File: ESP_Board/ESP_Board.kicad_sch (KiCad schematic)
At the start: 37 parts, among them J1 USB_C_Receptacle_USB2.0_14P, J2 Conn_01x18_Pin, J3 Conn_01x18_Pin, SW1 SW_Push, U1 ESP32-S3, U2 AMS1117, Y1 C1E-40.000-8-1010-R

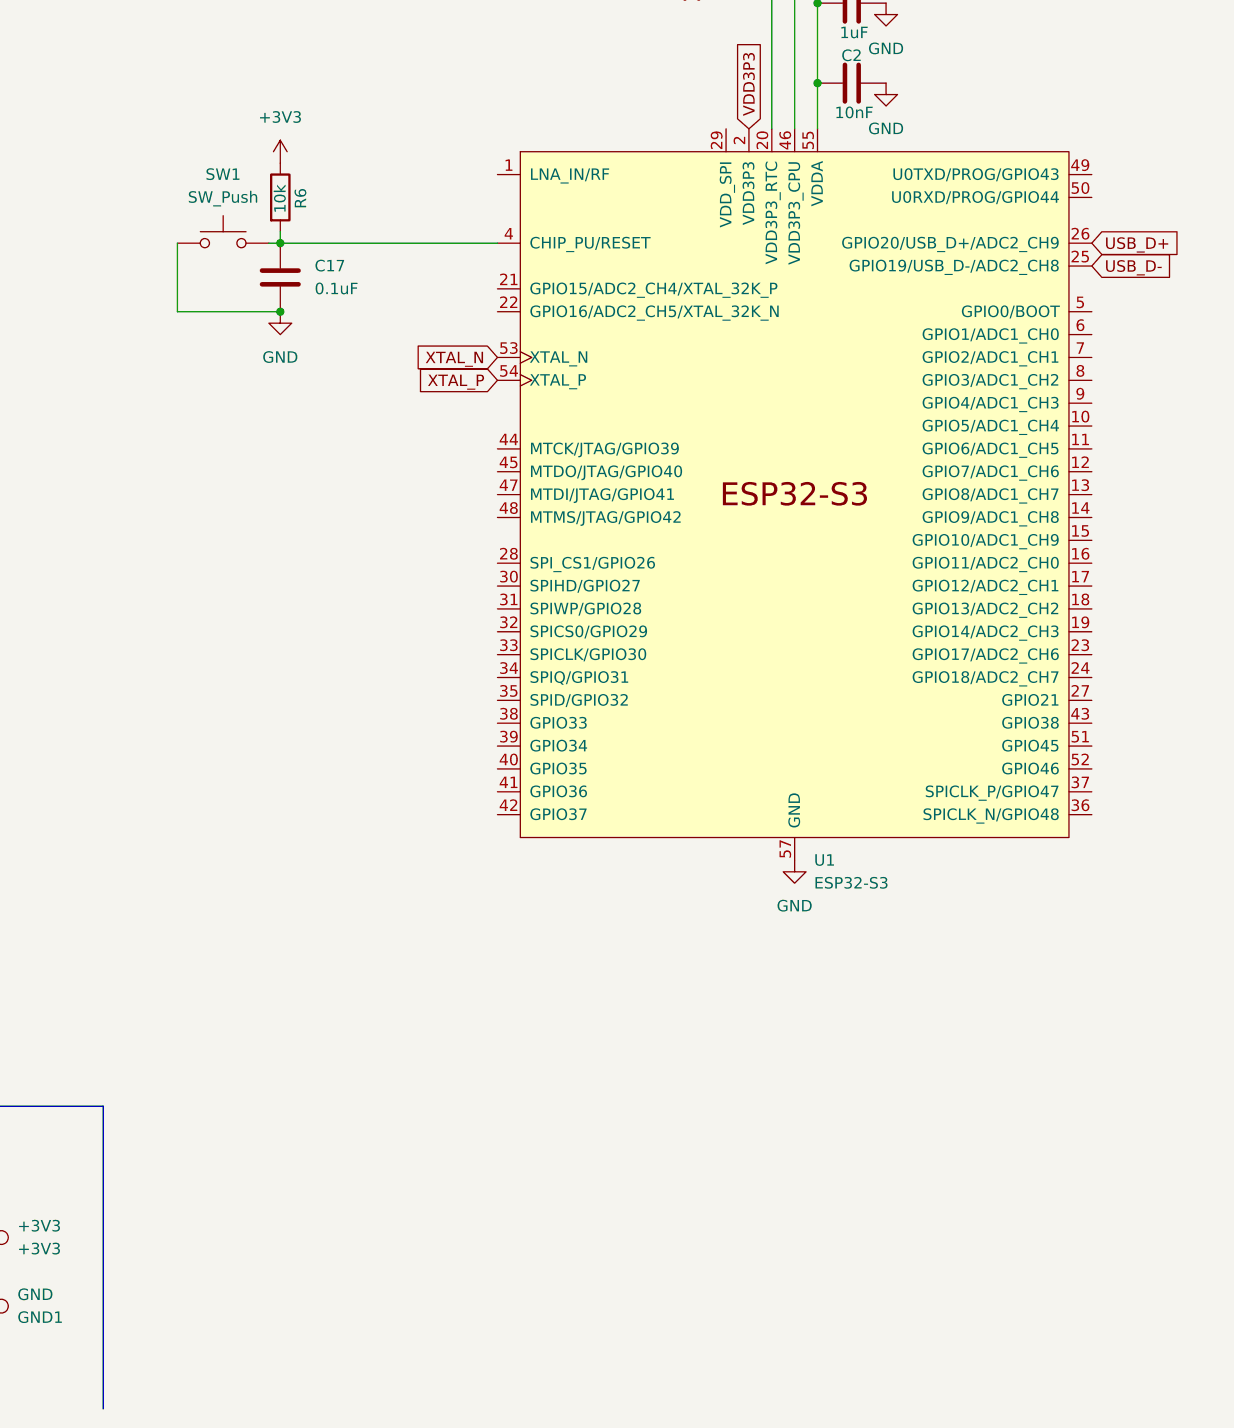
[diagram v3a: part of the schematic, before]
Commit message: Added BOOT button
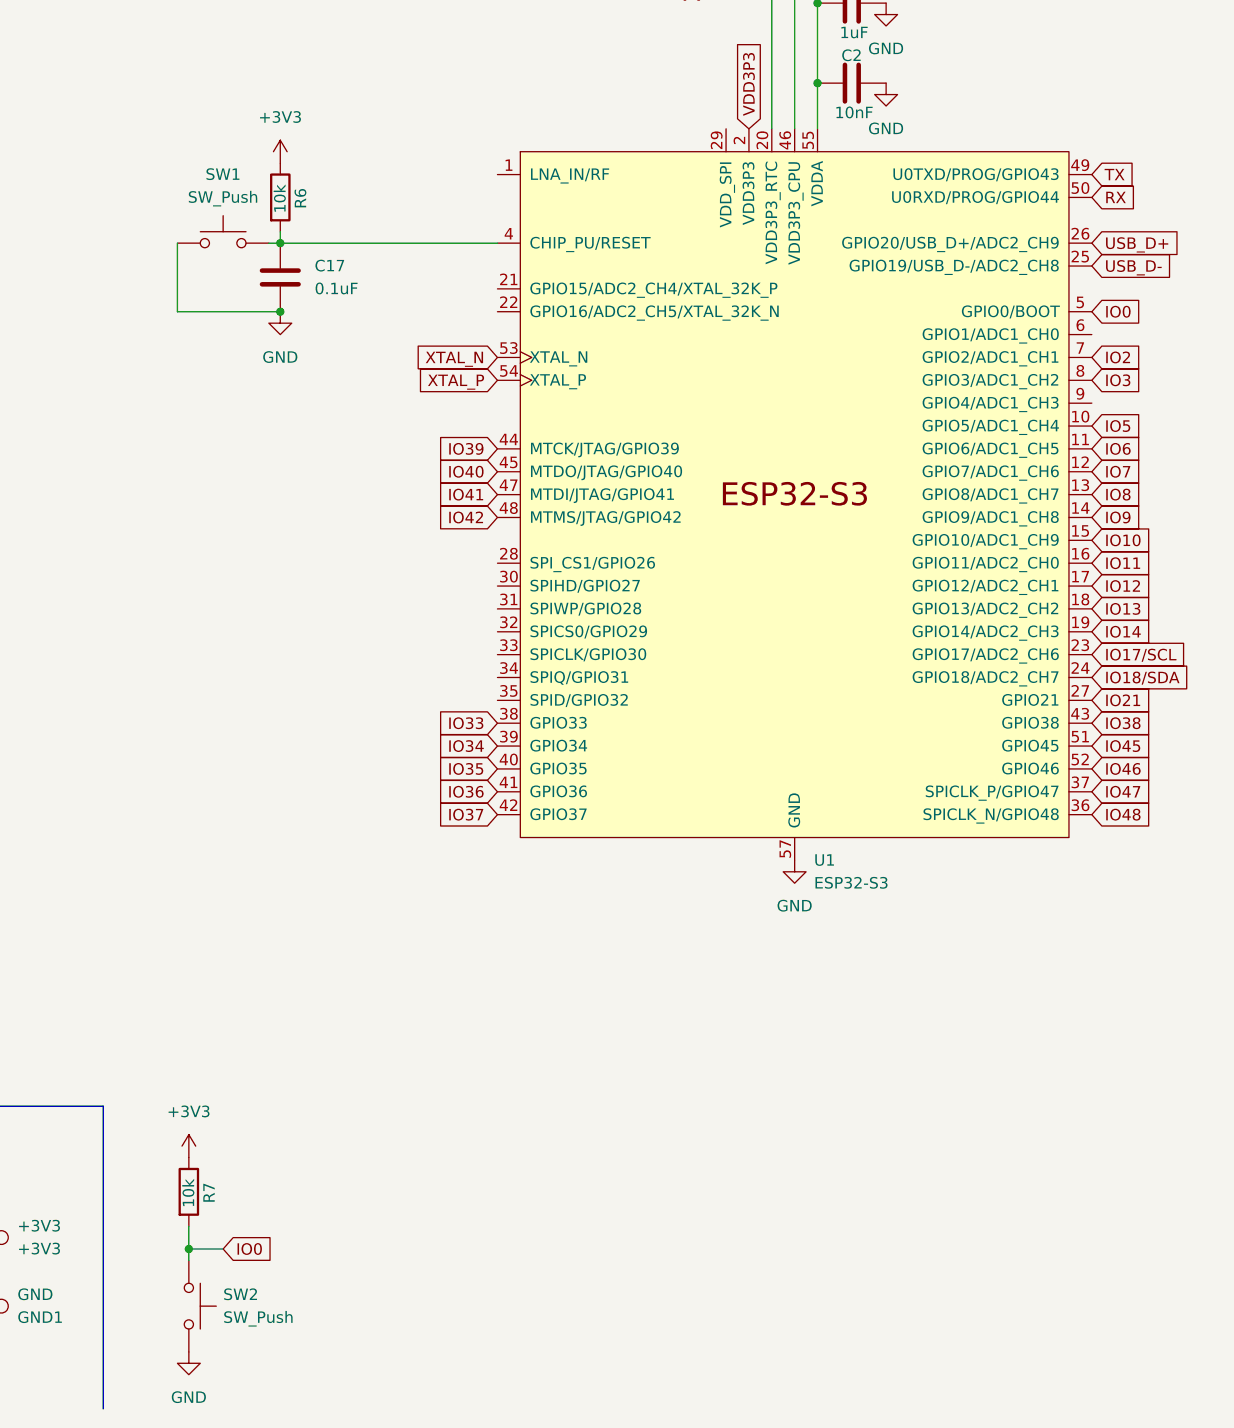
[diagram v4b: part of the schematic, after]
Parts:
- added R7: 10k, symbol Device:R
- added SW2: SW_Push, symbol Switch:SW_Push
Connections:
- net +3V3: now also R7.1
- net GND: now also SW2.2
- net IO0: now also U1.5 (GPIO0/BOOT), R7.2, SW2.1
- net IO10: now also U1.15 (GPIO10/ADC1_CH9)
- net IO11: now also U1.16 (GPIO11/ADC2_CH0)
- net IO12: now also U1.17 (GPIO12/ADC2_CH1)
- net IO13: now also U1.18 (GPIO13/ADC2_CH2)
- net IO14: now also U1.19 (GPIO14/ADC2_CH3)
- net IO17/SCL: now also U1.23 (GPIO17/ADC2_CH6)
- net IO18/SDA: now also U1.24 (GPIO18/ADC2_CH7)
- net IO2: now also U1.7 (GPIO2/ADC1_CH1)
- net IO21: now also U1.27 (GPIO21)
- net IO3: now also U1.8 (GPIO3/ADC1_CH2)
- net IO33: now also U1.38 (GPIO33)
- net IO34: now also U1.39 (GPIO34)
- net IO35: now also U1.40 (GPIO35)
- net IO36: now also U1.41 (GPIO36)
- net IO37: now also U1.42 (GPIO37)
- net IO38: now also U1.43 (GPIO38)
- net IO39: now also U1.44 (MTCK/JTAG/GPIO39)
- net IO40: now also U1.45 (MTDO/JTAG/GPIO40)
- net IO41: now also U1.47 (MTDI/JTAG/GPIO41)
- net IO42: now also U1.48 (MTMS/JTAG/GPIO42)
- net IO45: now also U1.51 (GPIO45)
- net IO46: now also U1.52 (GPIO46)
- net IO47: now also U1.37 (SPICLK_P/GPIO47)
- net IO48: now also U1.36 (SPICLK_N/GPIO48)
- net IO5: now also U1.10 (GPIO5/ADC1_CH4)
- net IO6: now also U1.11 (GPIO6/ADC1_CH5)
- net IO7: now also U1.12 (GPIO7/ADC1_CH6)
- net IO8: now also U1.13 (GPIO8/ADC1_CH7)
- net IO9: now also U1.14 (GPIO9/ADC1_CH8)
- net RX: now also U1.50 (U0RXD/PROG/GPIO44)
- net TX: now also U1.49 (U0TXD/PROG/GPIO43)

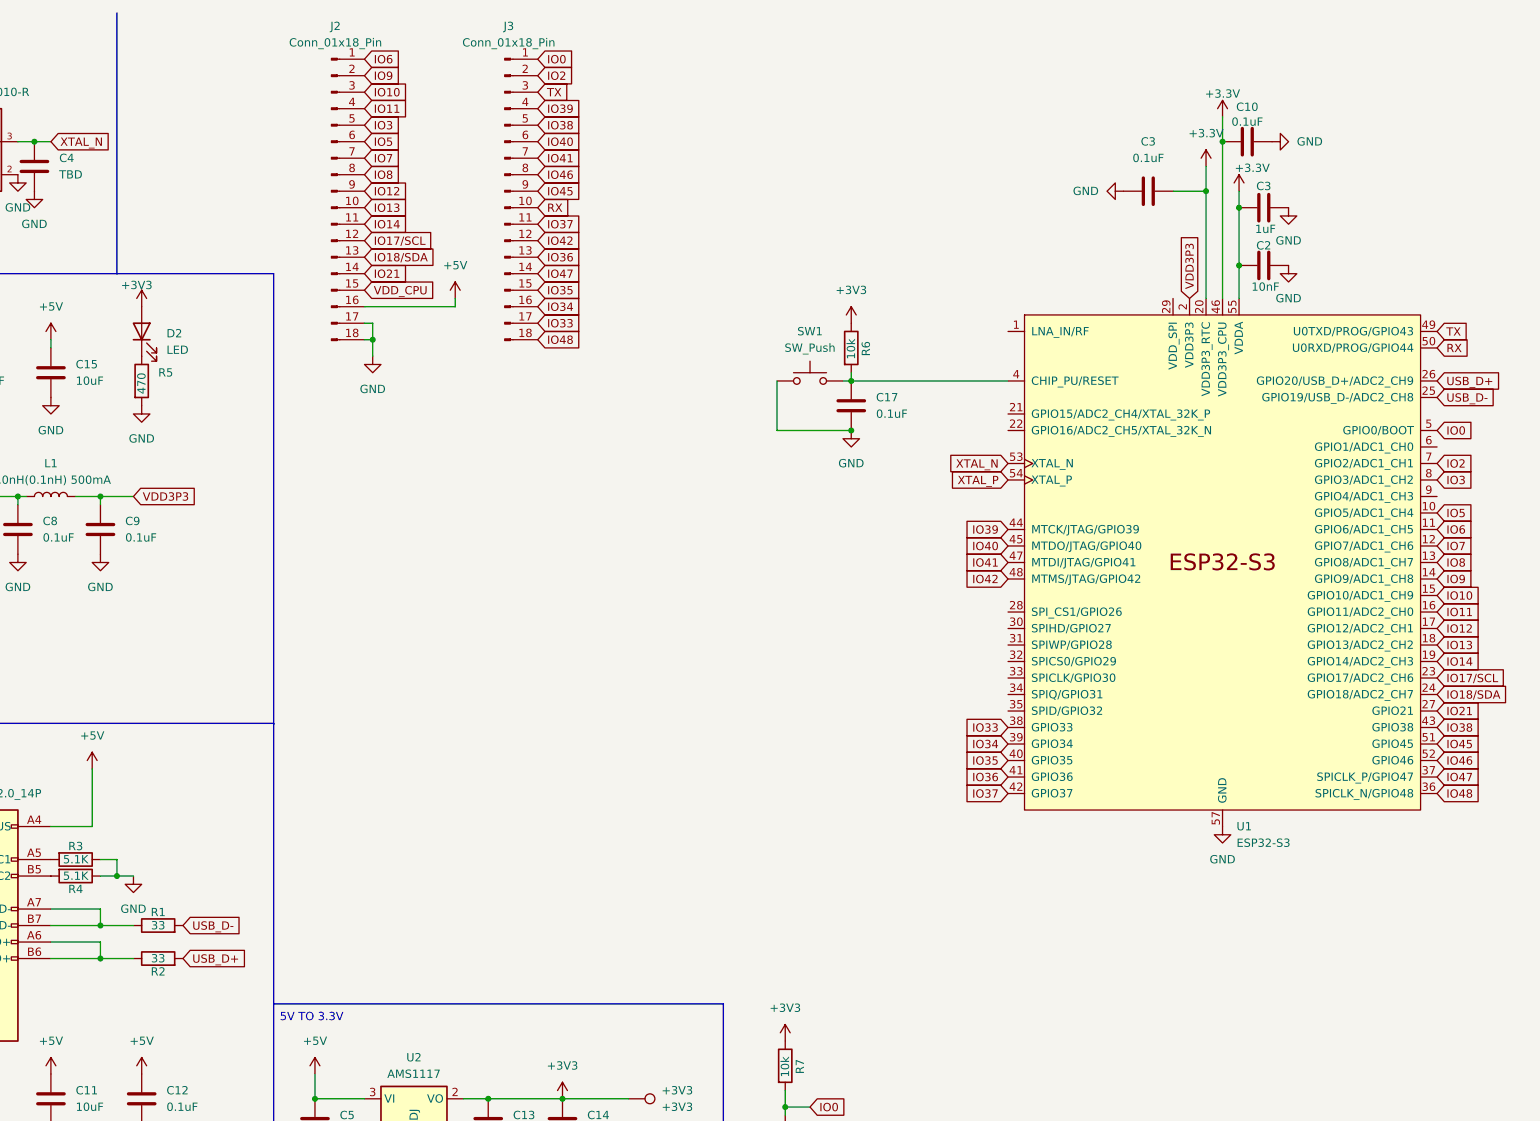
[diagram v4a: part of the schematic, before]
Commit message: Added antenna & memory, need to do impedance matching :(
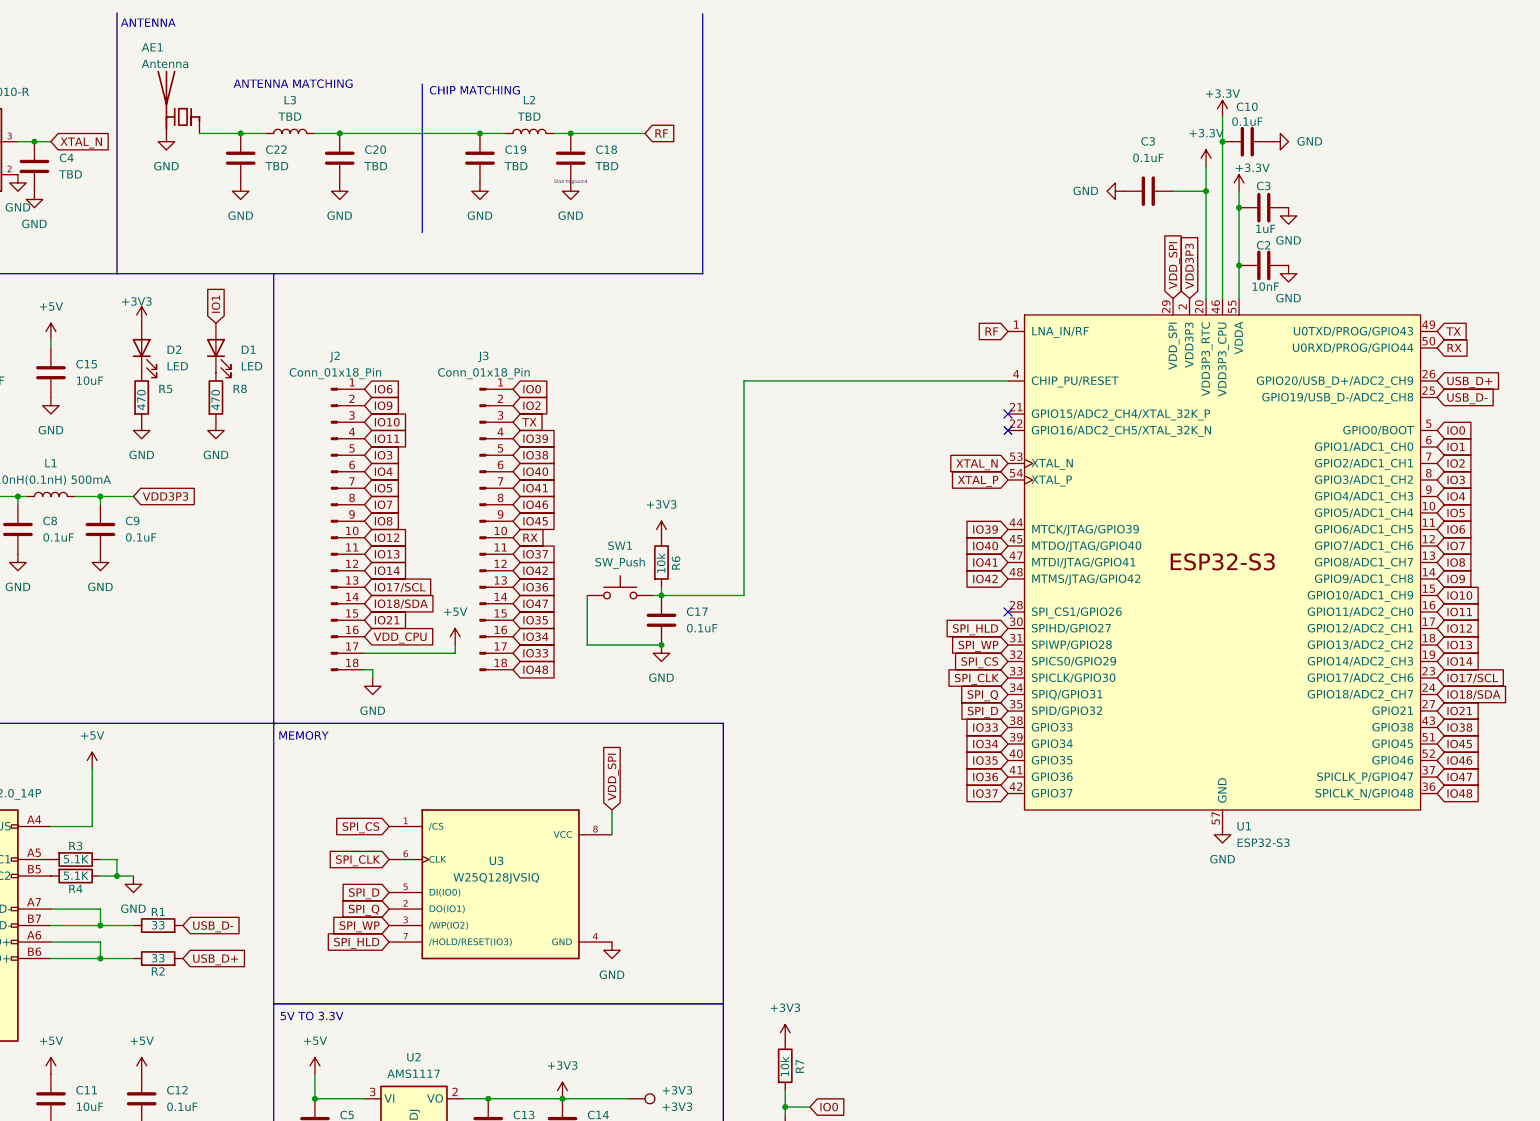
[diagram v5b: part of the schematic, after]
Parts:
- added AE1: Antenna, symbol Device:Antenna_Chip
- added C18, C19, C20, C22: TBD, symbol Device:C
- added D1: LED, symbol Device:LED
- added L2, L3: TBD, symbol Device:L
- added R8: 470, symbol Device:R
- added U3: W25Q128JVSIQ, W25Q128JVSIQ:SOIC127P790X216-8N, symbol Necessary_Imports:W25Q128JVSIQ
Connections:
- net +5V: now also J2.17 (Pin_17); no longer J2.16 (Pin_16)
- net GND: now also AE1.2 (PCB_Trace), C18.2, C19.2, C20.2, C22.2, R8.2, U3.4 (GND); no longer J2.17 (Pin_17)
- net IO12: now also J2.10 (Pin_10); no longer J2.9 (Pin_9)
- net IO13: now also J2.11 (Pin_11); no longer J2.10 (Pin_10)
- net IO14: now also J2.12 (Pin_12); no longer J2.11 (Pin_11)
- net IO17/SCL: now also J2.13 (Pin_13); no longer J2.12 (Pin_12)
- net IO18/SDA: now also J2.14 (Pin_14); no longer J2.13 (Pin_13)
- net IO21: now also J2.15 (Pin_15); no longer J2.14 (Pin_14)
- net IO5: now also J2.7 (Pin_7); no longer J2.6 (Pin_6)
- net IO7: now also J2.8 (Pin_8); no longer J2.7 (Pin_7)
- net IO8: now also J2.9 (Pin_9); no longer J2.8 (Pin_8)
- net VDD_CPU: now also J2.16 (Pin_16); no longer J2.15 (Pin_15)
- net RF: now reaches U1.1 (LNA_IN/RF)
- net RF: now also C18.1, L2.2
- net VDD_SPI: now reaches U1.29 (VDD_SPI)
- net VDD_SPI: now also U3.8 (VCC)
- net SPI_HLD: now reaches U1.30 (SPIHD/GPIO27)
- net SPI_HLD: now also U3.7 (/HOLD/RESET(IO3))
- net SPI_WP: now reaches U1.31 (SPIWP/GPIO28)
- net SPI_WP: now also U3.3 (/WP(IO2))
- net SPI_CS: now reaches U1.32 (SPICS0/GPIO29)
- net SPI_CS: now also U3.1 (/CS)
- net SPI_CLK: now reaches U1.33 (SPICLK/GPIO30)
- net SPI_CLK: now also U3.6 (CLK)
- net SPI_Q: now reaches U1.34 (SPIQ/GPIO31)
- net SPI_Q: now also U3.2 (DO(IO1))
- net SPI_D: now reaches U1.35 (SPID/GPIO32)
- net SPI_D: now also U3.5 (DI(IO0))
- net IO1: now reaches U1.6 (GPIO1/ADC1_CH0)
- net IO1: now also D1.2 (A)
- net IO4: now reaches U1.9 (GPIO4/ADC1_CH3)
- net IO4: now also J2.6 (Pin_6)
- new net: C19.1, C20.1, L2.1, L3.2
- new net: AE1.1 (FEED), C22.1, L3.1
- new net: D1.1 (K), R8.1
- no-connect marks 0 -> 3
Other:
- note added: "ANTENNA"
- note added: "ANTENNA MATCHING"
- note added: "CHIP MATCHING"
- note added: "MEMORY"
- note added: "Stub to ground"
- moved on the sheet: C17, D2, J2, J3, R5, R6, SW1
